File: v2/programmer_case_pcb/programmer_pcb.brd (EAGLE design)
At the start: 100 x 80 mm, 17 parts, among them J1 1X2-3.5MM, SW1 SPST_TACT-EVQQ2

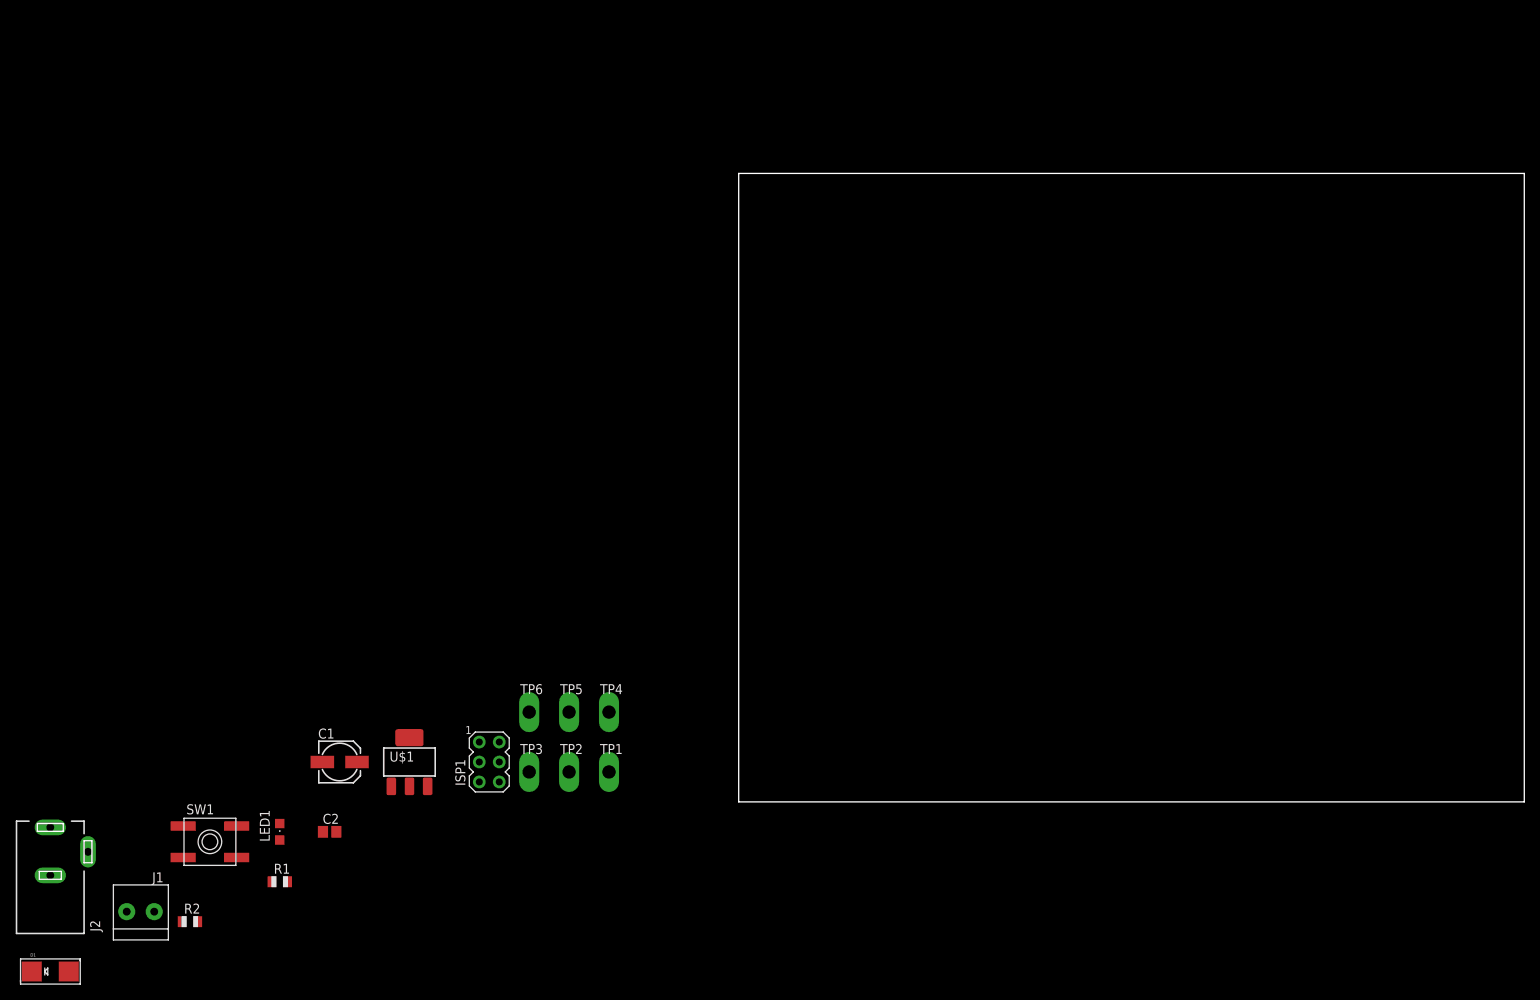
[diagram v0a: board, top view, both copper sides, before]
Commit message: start populating some of the components
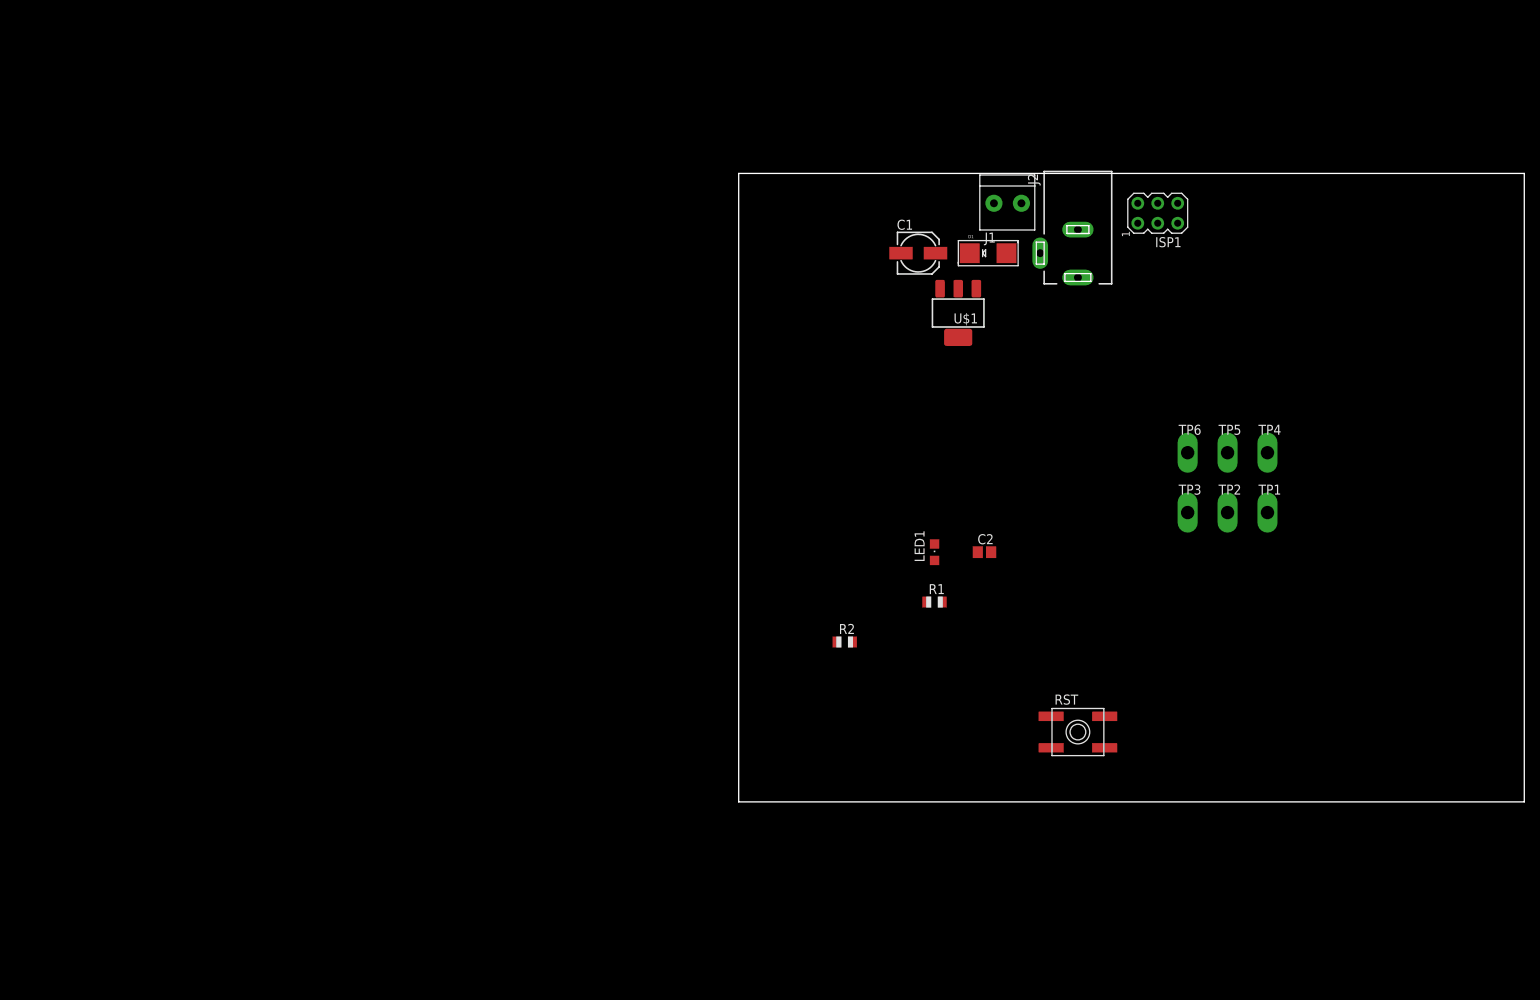
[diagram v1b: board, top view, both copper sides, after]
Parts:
- removed SW1: SPST_TACT-EVQQ2, adafruit:EVQ-Q2
- added RST: SPST_TACT-EVQQ2, adafruit:EVQ-Q2
- moved J2 151.4 mm to (43.2, 69.8), turned to 180 degrees
- moved D1 150.4 mm to (31.8, 69.8)
- moved J1 142.6 mm to (34.3, 76.2), turned to 180 degrees
- moved ISP1 110.1 mm to (53.3, 74.9), turned to 90 degrees
- moved C1 98.1 mm to (22.9, 69.8)
- moved C2 90.6 mm to (31.3, 31.8)
- moved LED1 90.6 mm to (24.9, 31.8)
- moved R1 90.6 mm to (24.9, 25.4)
- moved R2 90.6 mm to (13.5, 20.4)
- moved U$1 90.3 mm to (27.9, 62.2), turned to 180 degrees
- moved TP1 90.1 mm to (67.3, 36.8)
- moved TP4 90.1 mm to (67.3, 44.5)
- moved TP2 90.1 mm to (62.2, 36.8)
- moved TP3 90.1 mm to (57.1, 36.8)
- moved TP5 90.1 mm to (62.2, 44.5)
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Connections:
- net GND: now also RST.A, RST.A'; no longer SW1.A, SW1.A'
- net RESET: now also RST.B, RST.B'; no longer SW1.B, SW1.B'

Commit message: WIP
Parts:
- moved RST 79.7 mm to (62.2, 86.3)
- moved R1 57.2 mm to (32.4, 82.1)
- moved R2 57.2 mm to (21.0, 77.0)
- moved C2 57.2 mm to (38.7, 88.5)
- moved LED1 57.2 mm to (32.4, 88.5)
- moved TP1 52.4 mm to (80.7, 87.5)
- moved TP2 52.4 mm to (75.6, 87.5)
- moved TP3 52.4 mm to (70.5, 87.5)
- moved TP4 52.4 mm to (80.7, 95.1)
- moved TP5 52.4 mm to (75.6, 95.1)
- moved TP6 52.4 mm to (70.5, 95.1)
- moved C1 23.9 mm to (18.3, 93.3)
- moved D1 23.9 mm to (27.2, 93.3)
- moved U$1 23.9 mm to (23.4, 85.7)
- moved ISP1 22.7 mm to (61.4, 96.1)
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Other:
- board size 100 x 80 mm -> 100 x 100 mm

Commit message: finish the design
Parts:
- removed LED1: (no value), adafruit:CHIPLED_0805
- removed TP1, TP2, TP3, TP4, TP5, TP6: PTR1PAD1-17Y, testpad:P1-17Y
- removed U$1: LD1117, LD1117:SOT223
- added 5VREG: LD1117, LD1117:SOT223
- added H1, H2, H3, H4: MOUNT-HOLE3.2, holes:3,2
- added PWR: (no value), adafruit:CHIPLED_0805
- added TP_+5V, TP_GND, TP_MISO, TP_MOSI, TP_RST, TP_SCK: TPSQPAD1-13Y, testpad:P1-13Y
- C1: value 0.33 -> 0.33u
- C2: value 0.1 -> 0.1u
- R1: value (none) -> 10K
- moved RST 82.2 mm to (50.0, 5.00)
- moved R2 81.0 mm to (58.0, 5.00), turned to 270 degrees
- moved R1 78.7 mm to (42.0, 4.00), turned to 270 degrees
- moved C1 35.6 mm to (51.7, 80.7), turned to 180 degrees
- moved D1 11.7 mm to (38.2, 89.3)
- moved C2 7.02 mm to (36.0, 82.0), turned to 90 degrees
- moved ISP1 1.00 mm to (60.4, 96.1)
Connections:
- removed net VCC: ISP1.2, TP1.TP
- net +5V: now also 5VREG.2, 5VREG.4, ISP1.2, TP_+5V.TP; no longer U$1.2, U$1.4
- net GND: now also 5VREG.1, PWR.C, TP_GND.TP; no longer LED1.C, TP2.TP, U$1.1
- net MISO: now also TP_MISO.TP; no longer TP5.TP
- net MOSI: now also TP_MOSI.TP; no longer TP4.TP
- net N$1: now also PWR.A; no longer LED1.A
- net RESET: now also TP_RST.TP; no longer TP3.TP
- net SCK: now also TP_SCK.TP; no longer TP6.TP
- net V+: now also 5VREG.3; no longer U$1.3
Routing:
- net RESET: track 0.00 -> 121.4 mm
- net MOSI: track 0.00 -> 81.6 mm
- net SCK: track 0.00 -> 78.3 mm
- net MISO: track 0.00 -> 74.9 mm
- net GND: track 0.00 -> 19.9 mm, vias 0 -> 4
- net V+: track 0.00 -> 19.4 mm
- net N$2: track 0.00 -> 18.7 mm
- net N$1: track 0.00 -> 3.43 mm
- added copper zone on layer 1, net +5V
- added copper zone on layer 16, net GND

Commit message: add zip with gerber files
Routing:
- net MOSI: track 81.6 -> 80.6 mm
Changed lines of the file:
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@@
 <setting verticaltext="up"/>
 </settings>
-<grid distance="0.1" unitdist="mm" unit="mm" style="lines" multiple="1" display="yes" altdistance="5" altunitdist="mil" altunit="mil"/>
+<grid distance="0.01" unitdist="mm" unit="mm" style="lines" multiple="1" display="yes" altdistance="5" altunitdist="mil" altunit="mil"/>
 <layers>
 <layer number="1" name="Top" color="4" fill="1" visible="yes" active="yes"/>
@@
 <contactref element="TP_MOSI" pad="TP"/>
 <contactref element="ISP1" pad="4"/>
-<wire x1="34.71" y1="32.755" x2="35.76435" y2="32.755" width="0.3048" layer="1"/>
-<wire x1="64.2876" y1="61.250025" x2="64.2876" y2="96.0546" width="0.3048" layer="1"/>
-<wire x1="64.2876" y1="96.0546" x2="61.9454" y2="96.0546" width="0.3048" layer="1"/>
+<wire x1="61.9454" y1="96.0546" x2="64.2876" y2="96.0546" width="0.3048" layer="1"/>
 <wire x1="60.623" y1="97.377" x2="60.43" y2="97.377" width="0.3048" layer="1"/>
 <wire x1="61.9454" y1="96.0546" x2="60.623" y2="97.377" width="0.3048" layer="1"/>
-<wire x1="34.71" y1="32.755" x2="35.792575" y2="32.755" width="0.3048" layer="1"/>
-<wire x1="35.792575" y1="32.755" x2="64.2876" y2="61.250025" width="0.3048" layer="1"/>
+<wire x1="64.2876" y1="61.1876" x2="35.85" y2="32.75" width="0.3048" layer="1"/>
+<wire x1="35.85" y1="32.75" x2="34.715" y2="32.75" width="0.3048" layer="1"/>
+<wire x1="34.715" y1="32.75" x2="34.71" y2="32.755" width="0.3048" layer="1"/>
+<wire x1="64.2876" y1="96.0546" x2="64.2876" y2="61.1876" width="0.3048" layer="1"/>
 </signal>
 <signal name="MISO">

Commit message: add the v3 version of the pcb
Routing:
- net GND: track 19.9 -> 13.1 mm, vias 4 -> 3
- net RESET: track 121.4 -> 116.4 mm
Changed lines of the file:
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@@
 <setting verticaltext="up"/>
 </settings>
-<grid distance="0.01" unitdist="mm" unit="mm" style="lines" multiple="1" display="yes" altdistance="5" altunitdist="mil" altunit="mil"/>
+<grid distance="1" unitdist="mm" unit="mm" style="lines" multiple="1" display="yes" altdistance="5" altunitdist="mil" altunit="mil"/>
 <layers>
 <layer number="1" name="Top" color="4" fill="1" visible="yes" active="yes"/>
@@
 <wire x1="43" y1="8.05" x2="43" y2="9.5" width="0.6096" layer="1"/>
 <via x="43" y="9.5" extent="1-16" drill="0.35"/>
-<wire x1="49" y1="3" x2="53.4" y2="3" width="0.6096" layer="1"/>
-<wire x1="46.6" y1="3" x2="49" y2="3" width="0.6096" layer="1"/>
-<via x="49" y="3" extent="1-16" drill="0.35"/>
+<wire x1="46.6" y1="3" x2="53.4" y2="3" width="0" layer="19" extent="1-1"/>
+<wire x1="43.05" y1="8" x2="46.6" y2="3" width="0" layer="19" extent="1-1"/>
 </signal>
 <signal name="RESET">
@@
 <contactref element="R2" pad="1"/>
 <contactref element="RST" pad="B'"/>
-<wire x1="53.4" y1="7" x2="57" y2="7" width="0.6096" layer="1"/>
-<wire x1="57" y1="7" x2="58" y2="6" width="0.6096" layer="1"/>
-<wire x1="46.6" y1="7" x2="53.4" y2="7" width="0.6096" layer="1"/>
 <wire x1="62.97" y1="62.47" x2="62.97" y2="94.837" width="0.3048" layer="1"/>
 <wire x1="34.71" y1="35.295" x2="35.795" y2="35.295" width="0.3048" layer="1"/>
@@
 <wire x1="32.3" y1="35.3" x2="34.705" y2="35.3" width="0.3048" layer="1"/>
 <wire x1="34.705" y1="35.3" x2="34.71" y2="35.295" width="0.3048" layer="1"/>
+<wire x1="46.6" y1="7" x2="53.4" y2="7" width="0.3048" layer="1"/>
+<wire x1="53.4" y1="7" x2="58" y2="6" width="0" layer="19" extent="1-1"/>
 </signal>
 <signal name="MOSI">
